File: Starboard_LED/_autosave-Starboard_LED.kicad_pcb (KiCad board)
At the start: 2 copper layers, 21.1 x 21 mm, 3 parts, among them J1 Conn_01x01_Male, J2 Conn_01x01_Male

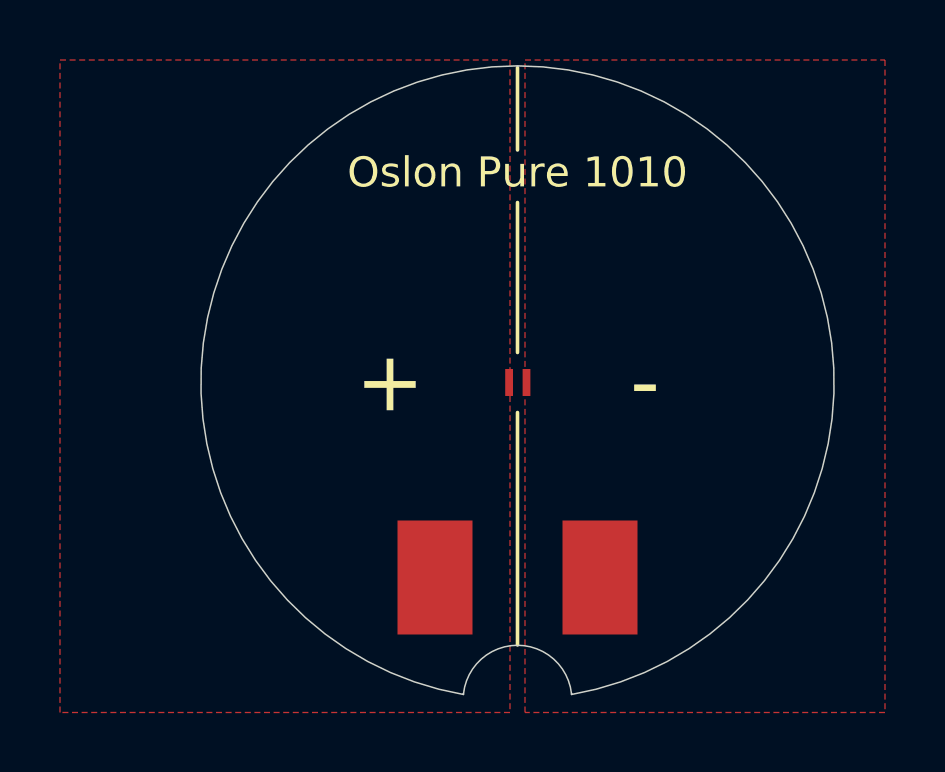
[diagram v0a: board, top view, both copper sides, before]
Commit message: Add Luxeon 2835
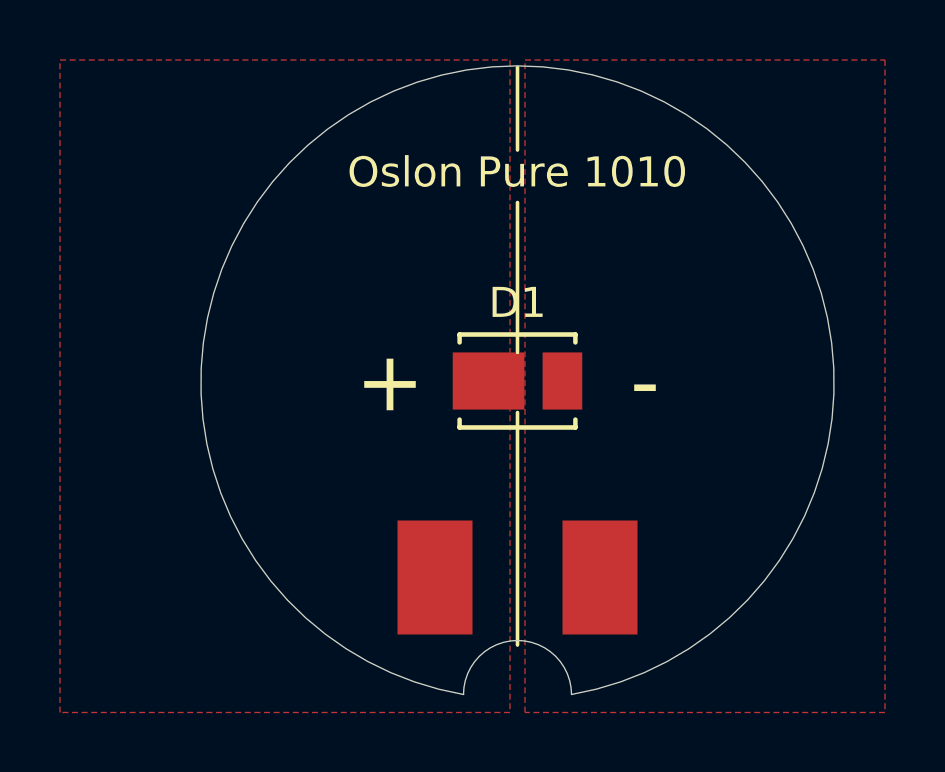
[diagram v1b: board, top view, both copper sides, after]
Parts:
- D1: footprint Custom:Oslon_Pure_1010 -> Custom:L128-BLU1003500000
- moved D1 0.28 mm to (157.5, 105.0), turned to 0 degrees
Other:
- outline, holes or cut-outs redrawn
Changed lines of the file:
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@@
   (general
     (thickness 1.6)
-    (drawings 15)
+    (drawings 13)
     (tracks 0)
     (zones 0)
@@
     (39 F.Mask user)
     (40 Dwgs.User user)
-    (41 Cmts.User user)
+    (41 Cmts.User user hide)
     (42 Eco1.User user)
     (43 Eco2.User user)
@@
     (add_net "Net-(D1-Pad2)")
   )
+  (module Custom:L128-BLU1003500000 (layer F.Cu)
+    (at 157.5 104.95)
+    (fp_text reference D1 (at 0 -2.6) (layer F.SilkS)
+      (effects (font (size 1 1) (thickness 0.15)))
+    )
+    (fp_text value LED (at 0.6 2.6) (layer Dwgs.User) hide
+      (effects (font (size 1 1) (thickness 0.15)))
+    )
+    (fp_text user "Copyright 2016 Accelerated Designs. All rights reserved." (at 0 0) (layer Cmts.User)
+      (effects (font (size 0.127 0.127) (thickness 0.002)))
+    )
+    (fp_line (start -1.8034 0.9525) (end -1.8034 -0.9525) (layer F.Fab) (width 0.1524))
+    (fp_line (start -1.8034 -0.9525) (end -1.8034 -0.9525) (layer F.Fab) (width 0.1524))
+    (fp_line (start -1.8034 -0.9525) (end -1.8034 0.9525) (layer F.Fab) (width 0.1524))
+    (fp_line (start -1.8034 0.9525) (end -1.8034 0.9525) (layer F.Fab) (width 0.1524))
+    (fp_line (start 1.8034 -0.9525) (end 1.8034 0.9525) (layer F.Fab) (width 0.1524))
+    (fp_line (start 1.8034 0.9525) (end 1.8034 0.9525) (layer F.Fab) (width 0.1524))
+    (fp_line (start 1.8034 0.9525) (end 1.8034 -0.9525) (layer F.Fab) (width 0.1524))
+    (fp_line (start 1.8034 -0.9525) (end 1.8034 -0.9525) (layer F.Fab) (width 0.1524))
+    (fp_line (start -2.413 1.2065) (end -2.413 -1.2065) (layer F.CrtYd) (width 0.1524))
+    (fp_line (start -2.413 -1.2065) (end -2.0574 -1.2065) (layer F.CrtYd) (width 0.1524))
+    (fp_line (start 2.0574 -1.2065) (end 2.413 -1.2065) (layer F.CrtYd) (width 0.1524))
+    (fp_line (start 2.413 -1.2065) (end 2.413 1.2065) (layer F.CrtYd) (width 0.1524))
+    (fp_line (start 2.413 1.2065) (end 2.0574 1.2065) (layer F.CrtYd) (width 0.1524))
+    (fp_line (start -2.0574 1.2065) (end -2.413 1.2065) (layer F.CrtYd) (width 0.1524))
+    (fp_line (start -2.0574 1.6764) (end -2.0574 1.2065) (layer F.CrtYd) (width 0.1524))
+    (fp_line (start -2.0574 -1.2065) (end -2.0574 -1.6764) (layer F.CrtYd) (width 0.1524))
+    (fp_line (start -2.0574 -1.6764) (end 2.0574 -1.6764) (layer F.CrtYd) (width 0.1524))
+    (fp_line (start 2.0574 -1.6764) (end 2.0574 -1.2065) (layer F.CrtYd) (width 0.1524))
+    (fp_line (start 2.0574 1.2065) (end 2.0574 1.6764) (layer F.CrtYd) (width 0.1524))
+    (fp_line (start 2.0574 1.6764) (end -2.0574 1.6764) (layer F.CrtYd) (width 0.1524))
+    (fp_line (start -1.9304 1.5494) (end 1.9304 1.5494) (layer F.SilkS) (width 0.1524))
+    (fp_line (start 1.9304 1.5494) (end 1.9304 1.28524) (layer F.SilkS) (width 0.1524))
+    (fp_line (start 1.9304 -1.5494) (end -1.9304 -1.5494) (layer F.SilkS) (width 0.1524))
+    (fp_line (start -1.9304 -1.5494) (end -1.9304 -1.28524) (layer F.SilkS) (width 0.1524))
+    (fp_line (start -1.8034 1.4224) (end 1.8034 1.4224) (layer F.Fab) (width 0.1524))
+    (fp_line (start 1.8034 1.4224) (end 1.8034 -1.4224) (layer F.Fab) (width 0.1524))
+    (fp_line (start 1.8034 -1.4224) (end -1.8034 -1.4224) (layer F.Fab) (width 0.1524))
+    (fp_line (start -1.8034 -1.4224) (end -1.8034 1.4224) (layer F.Fab) (width 0.1524))
+    (fp_line (start -1.9304 1.28524) (end -1.9304 1.5494) (layer F.SilkS) (width 0.1524))
+    (fp_line (start 1.9304 -1.28524) (end 1.9304 -1.5494) (layer F.SilkS) (width 0.1524))
+    (fp_circle (center -0.9652 0) (end -0.9652 0) (layer F.Fab) (width 0.1524))
+    (pad 1 smd rect (at -0.9652 0) (size 2.3876 1.905) (layers F.Cu F.Paste F.Mask)
+      (net 2 "Net-(D1-Pad1)"))
+    (pad 2 smd rect (at 1.4986 0) (size 1.3208 1.905) (layers F.Cu F.Paste F.Mask)
+      (net 1 "Net-(D1-Pad2)"))
+    (model :Downloads:ul_L128-BLU1003500000/LED_003500000_PLL.step
+      (at (xyz 0 0 0))
+      (scale (xyz 1 1 1))
+      (rotate (xyz 0 0 0))
+    )
+  )
   (module Custom:Starboard_wire_pad (layer F.Cu)
     (at 154.75 111.5 90)
@@
       (net 1 "Net-(D1-Pad2)") (zone_connect 1))
   )
-  (module Custom:Oslon_Pure_1010 (layer F.Cu)
-    (at 157.22 105 90)
-    (fp_text reference D1 (at 0.4 -1.6 90) (layer F.CrtYd)
-      (effects (font (size 1 1) (thickness 0.15)))
-    )
-    (fp_text value LED (at 0 2.8 90) (layer F.Fab)
-      (effects (font (size 1 1) (thickness 0.15)))
-    )
-    (pad 2 smd rect (at 0 0.58 90) (size 0.9 0.26) (layers F.Cu F.Paste F.Mask)
-      (net 1 "Net-(D1-Pad2)"))
-    (pad 1 smd rect (at 0 0 90) (size 0.9 0.26) (layers F.Cu F.Paste F.Mask)
-      (net 2 "Net-(D1-Pad1)"))
-    (model "${KIPRJMOD}/GG VJLPE1_F3_20200622_geometry.STEP"
-      (offset (xyz 0 -0.25 0))
-      (scale (xyz 1 1 1))
-      (rotate (xyz 0 0 0))
-    )
-  )
-  (gr_line (start 155.699999 115.399999) (end 155.700002 115.369998) (layer Edge.Cuts) (width 0.05))
-  (gr_line (start 159.299999 115.399999) (end 159.299998 115.37) (layer Edge.Cuts) (width 0.05))
+  (gr_arc (start 157.5 115.4) (end 155.7 115.4) (angle 180) (layer Edge.Cuts) (width 0.0001))
   (gr_line (start 155.75 115.25) (end 159.25 115.25) (layer Dwgs.User) (width 0.15))
-  (gr_arc (start 157.5 115.57) (end 159.299998 115.37) (angle -167.3195536) (layer Edge.Cuts) (width 0.05))
   (gr_line (start 157.5 97.25) (end 157.5 94.5) (layer F.SilkS) (width 0.12))
   (gr_line (start 157.5 104) (end 157.5 99) (layer F.SilkS) (width 0.12))
@@
   )
   (gr_line (start 157.5 106) (end 157.5 113.75) (layer F.SilkS) (width 0.12))
-  (gr_arc (start 157.5 105) (end 159.299999 115.399999) (angle -340.3613987) (layer Edge.Cuts) (width 0.05))
+  (gr_arc (start 157.5 105) (end 159.299999 115.399999) (angle -340.4) (layer Edge.Cuts) (width 0.0001))
   (gr_line (start 157.5 105) (end 157.5 115.5) (layer Dwgs.User) (width 0.15))
   (gr_line (start 157.5 105) (end 157.5 94.5) (layer Dwgs.User) (width 0.15))
